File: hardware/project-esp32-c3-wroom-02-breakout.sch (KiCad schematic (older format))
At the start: 29 parts, among them J1 SM04B-SRSS-TB(LF)(SN), J2 Conn_01x08_Male, J3 Conn_01x08_Male, J4 USB4105-GF-A, Q1 MUN5214DW1T1G, Q2 Q_PMOS_DGS, U1 XC6220B331MR, U2 ESP32-C3-WROOM-02-H4

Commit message: Change schottky footprint for non handsolder
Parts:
- D2: footprint Diode_SMD:D_SOD-323_HandSoldering -> Diode_SMD:D_SOD-323
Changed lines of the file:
@@
 F 0 "D2" H 1850 1383 50  0000 C CNN
 F 1 "CUS10S30,H3F‎" H 1850 1474 50  0000 C CNN
-F 2 "Diode_SMD:D_SOD-323_HandSoldering" H 1850 1600 50  0001 C CNN
+F 2 "Diode_SMD:D_SOD-323" H 1850 1600 50  0001 C CNN
 F 3 "~" H 1850 1600 50  0001 C CNN
 	1    1850 1600

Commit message: First placement done
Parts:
- J3: value Conn_01x08_Male -> Conn_01x10_Male; footprint Connector_PinHeader_2.54mm:PinHeader_1x08_P2.54mm_Vertical -> Connector_PinHeader_2.54mm:PinHeader_1x10_P2.54mm_Vertical; symbol Connector:Conn_01x08_Male -> Connector:Conn_01x10_Male
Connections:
- wire segments 137 -> 139
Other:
- moved on the sheet: J2
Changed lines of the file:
@@
 Comment4 ""
 $EndDescr
-Text Label 6000 7300 0    50   ~ 0
+Text Label 6000 7200 0    50   ~ 0
 RTS
-Text Label 6000 7200 0    50   ~ 0
+Text Label 6000 7100 0    50   ~ 0
 DTR
 $Comp
@@
 	3950 1600 3950 1400
 Connection ~ 3950 1600
-Text Label 6000 7100 0    50   ~ 0
+Text Label 6000 7000 0    50   ~ 0
 RX
-Text Label 6000 7000 0    50   ~ 0
+Text Label 6000 6900 0    50   ~ 0
 TX
 Text Label 1750 4500 0    50   ~ 0
@@
 Wire Wire Line
 	1750 4400 2050 4400
+Text Label 6000 6600 0    50   ~ 0
+GPIO0
+Wire Wire Line
+	6000 6600 6300 6600
 Text Label 6000 6700 0    50   ~ 0
-GPIO0
+GPIO1
 Wire Wire Line
 	6000 6700 6300 6700
-Text Label 6000 6800 0    50   ~ 0
-GPIO1
-Wire Wire Line
-	6000 6800 6300 6800
 Text Label 1750 4600 0    50   ~ 0
 GPIO3
@@
 Wire Wire Line
 	1750 4900 2050 4900
-Text Label 6000 6900 0    50   ~ 0
+Text Label 6000 6800 0    50   ~ 0
 GPIO3
 Wire Wire Line
-	6000 6900 6300 6900
+	6000 6800 6300 6800
+Text Label 5200 6800 0    50   ~ 0
+GPIO4
+Wire Wire Line
+	5200 6800 5500 6800
 Text Label 5200 6900 0    50   ~ 0
-GPIO4
+GPIO5
 Wire Wire Line
 	5200 6900 5500 6900
-Text Label 5200 7000 0    50   ~ 0
-GPIO5
 Wire Wire Line
 	5200 7000 5500 7000
-Wire Wire Line
-	5200 7100 5500 7100
 Wire Wire Line
 	3450 4300 3750 4300
@@
 GPIO10
 Wire Wire Line
-	6000 7400 6300 7400
-Text Label 6000 7400 0    50   ~ 0
+	6000 7300 6300 7300
+Text Label 6000 7300 0    50   ~ 0
 GPIO10
 $Comp
 L Connector:Conn_01x08_Male J2
 U 1 1 61A53595
-P 5700 7000
-F 0 "J2" H 5672 6928 50  0000 R CNN
-F 1 "Conn_01x08_Male" H 5672 6883 50  0001 R CNN
-F 2 "Connector_PinHeader_2.54mm:PinHeader_1x08_P2.54mm_Vertical" H 5700 7000 50  0001 C CNN
-F 3 "~" H 5700 7000 50  0001 C CNN
-	1    5700 7000
+P 5700 6900
+F 0 "J2" H 5672 6828 50  0000 R CNN
+F 1 "Conn_01x08_Male" H 5672 6783 50  0001 R CNN
+F 2 "Connector_PinHeader_2.54mm:PinHeader_1x08_P2.54mm_Vertical" H 5700 6900 50  0001 C CNN
+F 3 "~" H 5700 6900 50  0001 C CNN
+	1    5700 6900
 	-1   0    0    -1
 $EndComp
 Text Label 3800 1600 0    50   ~ 0
 3V3
-Text Label 5200 7400 0    50   ~ 0
+Text Label 5200 7300 0    50   ~ 0
 GND
-Wire Wire Line
-	5200 7400 5500 7400
 Text Label 3300 2100 0    50   ~ 0
 GND
 $Comp
-L Connector:Conn_01x08_Male J3
+L Connector:Conn_01x10_Male J3
 U 1 1 61AC5D2E
 P 6500 7000
 F 0 "J3" H 6472 6928 50  0000 R CNN
-F 1 "Conn_01x08_Male" H 6472 6883 50  0001 R CNN
-F 2 "Connector_PinHeader_2.54mm:PinHeader_1x08_P2.54mm_Vertical" H 6500 7000 50  0001 C CNN
+F 1 "Conn_01x10_Male" H 6472 6883 50  0001 R CNN
+F 2 "Connector_PinHeader_2.54mm:PinHeader_1x10_P2.54mm_Vertical" H 6500 7000 50  0001 C CNN
 F 3 "~" H 6500 7000 50  0001 C CNN
 	1    6500 7000
@@
 $EndComp
 Wire Wire Line
-	5200 7200 5500 7200
+	5200 7100 5500 7100
+Wire Wire Line
+	6000 7000 6300 7000
+Wire Wire Line
+	6000 6900 6300 6900
 Wire Wire Line
 	6000 7100 6300 7100
 Wire Wire Line
-	6000 7000 6300 7000
-Wire Wire Line
 	6000 7200 6300 7200
-Wire Wire Line
-	6000 7300 6300 7300
-Text Label 5200 6700 0    50   ~ 0
+Text Label 5200 6600 0    50   ~ 0
 3V3
 Wire Wire Line
-	5200 6700 5500 6700
+	5200 6600 5500 6600
 $Comp
 L power:+3.3V #PWR0113
@@
 Text Notes 7050 2850 0    50   ~ 0
 I2C/StemmaQT
-Text Label 5200 6800 0    50   ~ 0
+Text Label 5200 6700 0    50   ~ 0
 RESET
 Wire Wire Line
-	5200 6800 5500 6800
+	5200 6700 5500 6700
 $Comp
 L power:+3.3V #PWR0116
@@
 Text Label 3500 4300 0    50   ~ 0
 SCL
-Text Label 5200 7200 0    50   ~ 0
+Text Label 5200 7100 0    50   ~ 0
 SCL
 Text Label 1750 4900 0    50   ~ 0
 SDA
-Text Label 5200 7100 0    50   ~ 0
+Text Label 5200 7000 0    50   ~ 0
 SDA
 Wire Wire Line
@@
 $EndComp
 Wire Wire Line
-	5200 7300 5500 7300
-Text Label 5200 7300 0    50   ~ 0
+	5200 7200 5500 7200
+Text Label 5200 7200 0    50   ~ 0
 VBAT
 $Comp
@@
 Wire Notes Line
 	4650 5200 4650 7800
+Wire Wire Line
+	5200 7300 5500 7300
+Text Label 6000 7400 0    50   ~ 0
+GND
+Wire Wire Line
+	6000 7400 6300 7400
+Text Label 6000 7500 0    50   ~ 0
+GND
+Wire Wire Line
+	6000 7500 6300 7500
 $EndSCHEMATC

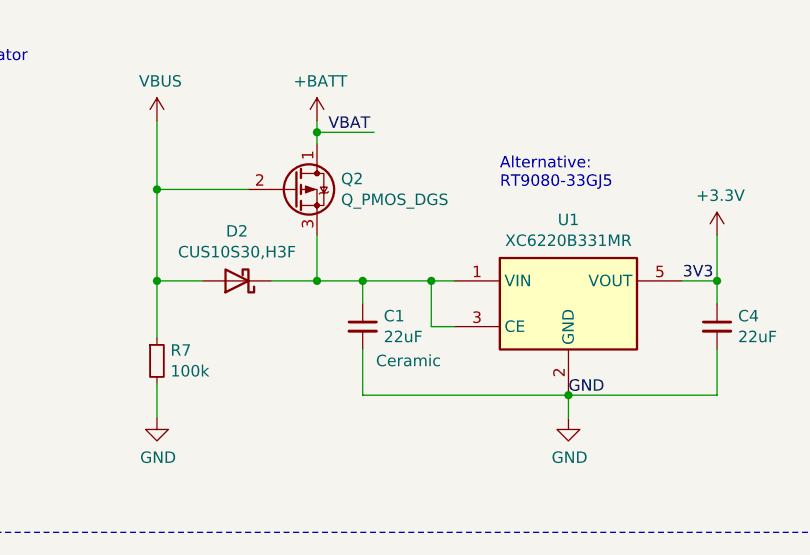
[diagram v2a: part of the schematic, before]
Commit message: Power + USB route
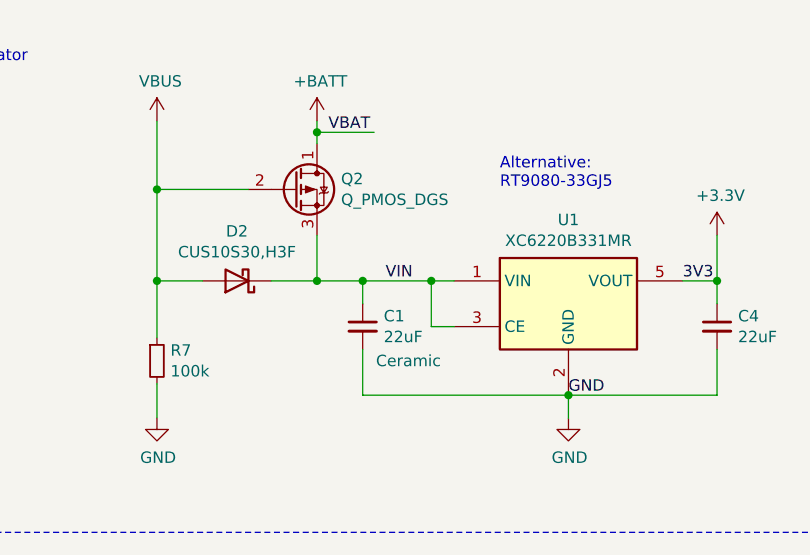
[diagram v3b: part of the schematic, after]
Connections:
- net labels added: VIN
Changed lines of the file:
@@
 Wire Wire Line
 	6000 7500 6300 7500
+Text Label 2500 1600 0    50   ~ 0
+VIN
 $EndSCHEMATC

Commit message: Routing done
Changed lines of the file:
@@
 Comment4 ""
 $EndDescr
+Text Label 6000 7100 0    50   ~ 0
+RTS
 Text Label 6000 7200 0    50   ~ 0
-RTS
-Text Label 6000 7100 0    50   ~ 0
 DTR
 $Comp
